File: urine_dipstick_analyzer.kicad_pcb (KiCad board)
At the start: 2 copper layers, 50 x 30 mm, 28 parts, among them J1 BAT, J2 9V_OUT, J3 3V3_OUT, J4 I2C_BUS, J5 MOTOR_PWR, U1 MCP73833, U1a USB-C-BO, U4 MAX17048

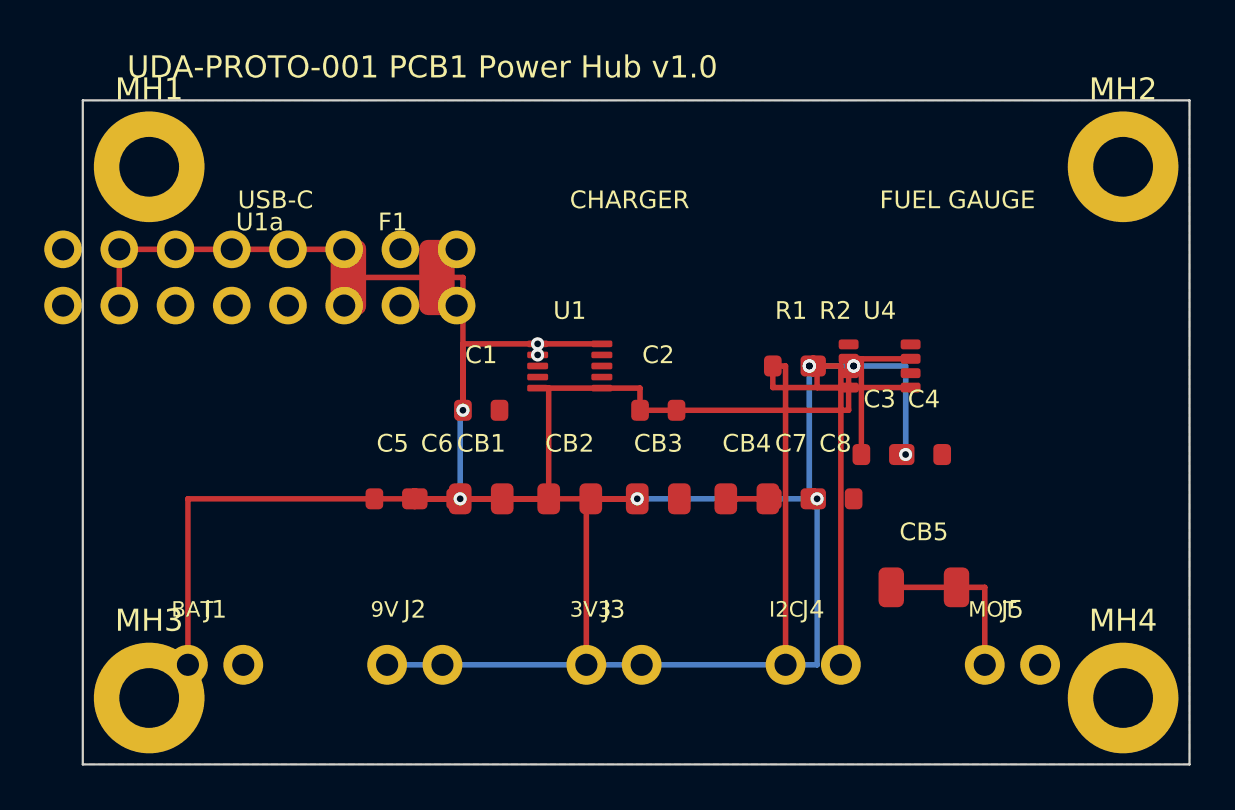
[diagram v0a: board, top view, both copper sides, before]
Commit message: Add STATUS.md: honest accounting of working vs unfinished assets
DRC/ERC findings:
- Schematic: 252 ERC violations (unconnected pins on auto-placed passives)
- PCB: 75 DRC violations (footprint mismatches, mask bridges) + 51 unrouted nets
- Generator approach hit its limit — PCB needs human KiCad work

Stripped the bad autorouted tracks (46 segments, 11 vias) since they
introduced shorts. PCB is back to a clean unrouted placement.
Gerbers regenerated but flagged not-manufacturable until DRC clean.

Committed reports (drc_report.txt, erc_report.txt) so reviewer can see
exact issue list. STATUS.md documents recommended path forward.

Co-Authored-By: Claude Opus 4.6 <noreply@anthropic.com>
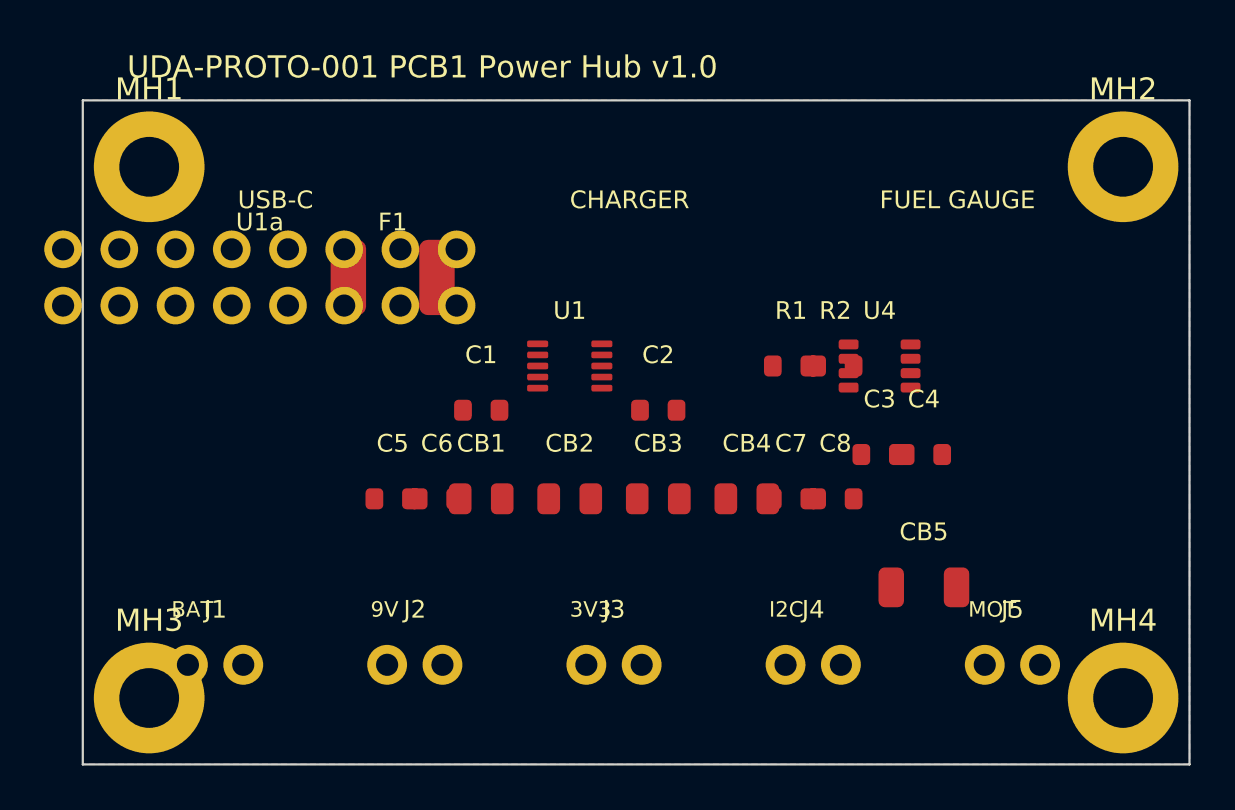
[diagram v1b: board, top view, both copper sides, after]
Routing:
- net VBAT: track 54.4 -> 0.00 mm
- net +3V3: track 41.8 -> 0.00 mm, vias 6 -> 0
- net VBUS: track 38.7 -> 0.00 mm, vias 2 -> 0
- net +9V: track 26.9 -> 0.00 mm, vias 1 -> 0
- net SCL: track 19.8 -> 0.00 mm
- net SDA: track 18.5 -> 0.00 mm
- net VMOT: track 7.73 -> 0.00 mm
- net +5V: track 2.12 -> 0.00 mm
- net CHRG_STAT: track 0.50 -> 0.00 mm, vias 2 -> 0
